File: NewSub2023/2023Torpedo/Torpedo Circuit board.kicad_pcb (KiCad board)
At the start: 2 copper layers, 18 x 18 mm, 7 parts

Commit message: added text to board
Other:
- board text added: "Nathaniel Oftedal v 1.0"
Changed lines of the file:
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@@
   (gr_circle (center 144.5 112.1) (end 153.5 112.1)
     (stroke (width 0.1) (type default)) (fill none) (layer "Edge.Cuts"))
+  (gr_text "Nathaniel Oftedal v 1.0" (at 137.4 114.9) (layer "F.SilkS")
+    (effects (font (size 0.8 0.8) (thickness 0.1)) (justify left bottom))
+  )
   (dimension (type aligned) (layer "Dwgs.User")
     (pts (xy 144.5 103.1) (xy 144.5 110.7))

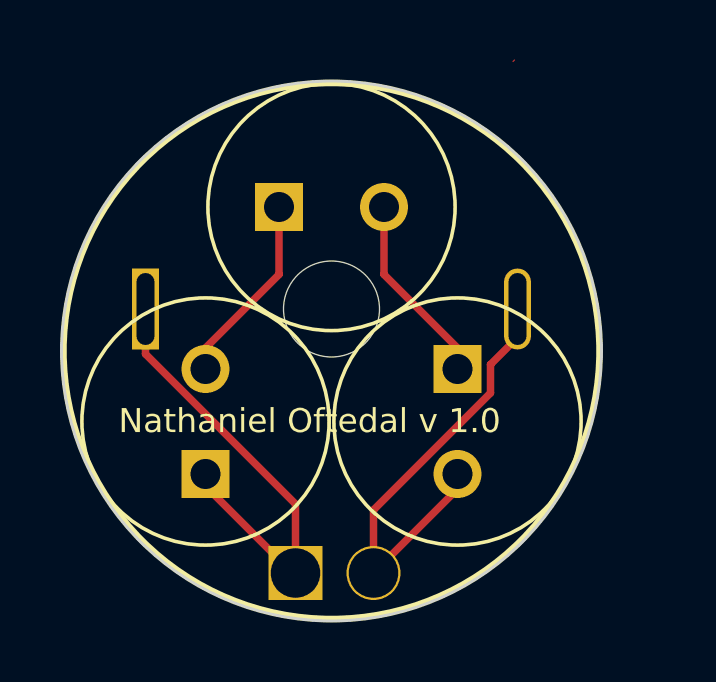
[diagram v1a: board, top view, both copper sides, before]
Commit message: Changed Torpedo circuit board wire thickness
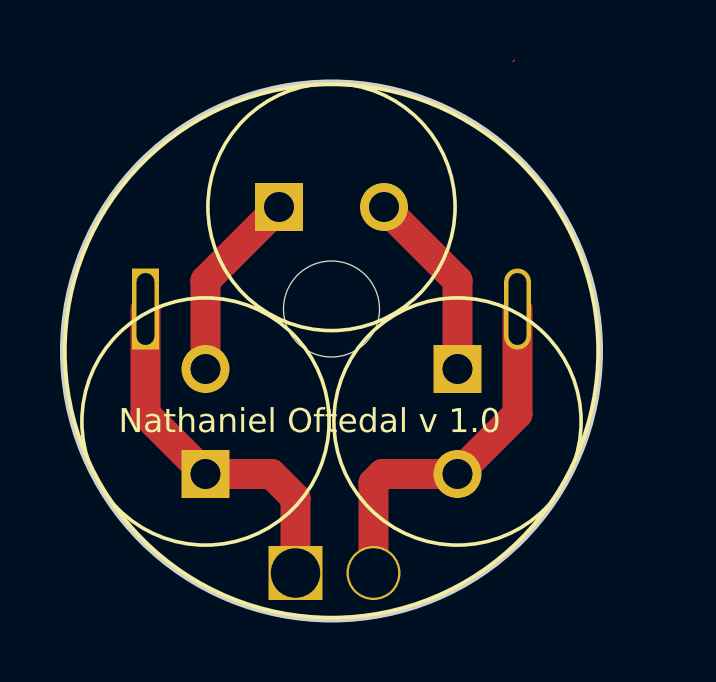
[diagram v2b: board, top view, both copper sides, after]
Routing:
- net (no net): track 43.6 -> 37.6 mm
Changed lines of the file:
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@@
       (outputformat 1)
       (mirror false)
-      (drillshape 1)
+      (drillshape 0)
       (scaleselection 1)
-      (outputdirectory "")
+      (outputdirectory "../../../OneDrive/Desktop/PCB Gerbers/")
     )
   )
@@
     (style (thickness 0.15) (arrow_length 1.27) (text_position_mode 0) (extension_height 0.58642) (extension_offset 0.5) keep_text_aligned)
   )
-  (segment (start 148.7 116.7) (end 145.9 119.5) (width 0.25) (layer "F.Cu") (net 0))
-  (segment (start 138.3 112.2) (end 138.3 110.7) (width 0.25) (layer "F.Cu") (net 0))
-  (segment (start 140.3 112) (end 142.75 109.55) (width 0.25) (layer "F.Cu") (net 0))
-  (segment (start 143.3 119.5) (end 143.2 119.5) (width 0.25) (layer "F.Cu") (net 0))
-  (segment (start 149.8 113.5) (end 149.8 112.55) (width 0.25) (layer "F.Cu") (net 0))
-  (segment (start 150.7 111.65) (end 150.7 110.7) (width 0.25) (layer "F.Cu") (net 0))
-  (segment (start 146.25 107.3) (end 146.25 109.55) (width 0.25) (layer "F.Cu") (net 0))
+  (segment (start 140.3 112.7) (end 140.3 109.75) (width 1) (layer "F.Cu") (net 0))
+  (segment (start 148.7 109.75) (end 148.7 112.7) (width 1) (layer "F.Cu") (net 0))
+  (segment (start 148.7 116.2) (end 146.2 116.2) (width 1) (layer "F.Cu") (net 0))
   (segment (start 150.55 102.45) (end 150.6 102.4) (width 0) (layer "F.Cu") (net 0))
-  (segment (start 148.7 112) (end 148.7 112.7) (width 0.25) (layer "F.Cu") (net 0))
-  (segment (start 145.9 119.5) (end 145.9 117.4) (width 0.25) (layer "F.Cu") (net 0))
-  (segment (start 142.75 109.55) (end 142.75 107.3) (width 0.25) (layer "F.Cu") (net 0))
-  (segment (start 148.7 116.2) (end 148.7 116.7) (width 0.25) (layer "F.Cu") (net 0))
-  (segment (start 143.3 119.5) (end 143.3 117.2) (width 0.25) (layer "F.Cu") (net 0))
-  (segment (start 140.3 112.7) (end 140.3 112) (width 0.25) (layer "F.Cu") (net 0))
-  (segment (start 145.9 117.4) (end 149.8 113.5) (width 0.25) (layer "F.Cu") (net 0))
-  (segment (start 146.25 109.55) (end 148.7 112) (width 0.25) (layer "F.Cu") (net 0))
-  (segment (start 140.3 116.6) (end 140.3 116.2) (width 0.25) (layer "F.Cu") (net 0))
-  (segment (start 149.8 112.55) (end 150.7 111.65) (width 0.25) (layer "F.Cu") (net 0))
-  (segment (start 143.2 119.5) (end 140.3 116.6) (width 0.25) (layer "F.Cu") (net 0))
-  (segment (start 143.3 117.2) (end 138.3 112.2) (width 0.25) (layer "F.Cu") (net 0))
+  (segment (start 143.3 117) (end 142.5 116.2) (width 1) (layer "F.Cu") (net 0))
+  (segment (start 150.7 110.7) (end 150.7 114.2) (width 1) (layer "F.Cu") (net 0))
+  (segment (start 146.2 116.2) (end 145.9 116.5) (width 1) (layer "F.Cu") (net 0))
+  (segment (start 145.9 116.5) (end 145.9 119.5) (width 1) (layer "F.Cu") (net 0))
+  (segment (start 143.3 119.5) (end 143.3 117) (width 1) (layer "F.Cu") (net 0))
+  (segment (start 150.7 114.2) (end 148.7 116.2) (width 1) (layer "F.Cu") (net 0))
+  (segment (start 138.3 110.7) (end 138.3 114.2) (width 1) (layer "F.Cu") (net 0))
+  (segment (start 146.25 107.3) (end 148.7 109.75) (width 1) (layer "F.Cu") (net 0))
+  (segment (start 140.3 109.75) (end 142.75 107.3) (width 1) (layer "F.Cu") (net 0))
+  (segment (start 138.3 114.2) (end 140.3 116.2) (width 1) (layer "F.Cu") (net 0))
+  (segment (start 142.5 116.2) (end 140.3 116.2) (width 1) (layer "F.Cu") (net 0))
+  (segment (start 140.3 116.2) (end 140.3 116.5) (width 1) (layer "F.Cu") (net 0))
 )
